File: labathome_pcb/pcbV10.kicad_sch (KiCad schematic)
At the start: 118 parts, among them J1 PROG, J10 Fan1, J11 Fan2, J12 VPS, J15 1B 2A, J18 Power, J2 Srvo, J20 FAN5V, J3 I2C, J4 1wire, J5 EXT, J6 5V 3V GN 24, J7 485, J9 GN 5V RGB GN, K1 G6K-2, K2 G6K-2, K3 G6K-2, Q1 BC817, Q2 BC817, Q4 BC817, Q5 IRLML6344, Q6 BC817, Q7 TIP41, Q9 IRLML6344, SW1 BTN BLUE, SW10 5V FAN 24V, SW12 RESET, SW2 YELLOW, SW3 GREEN, SW4 RED, SW5 BTN WHITE, SW6 OFF TERM ON, SW7 LED HTR, SW8 REL ROT, SW9 SNS MOV, U1 AMS1117, U14 IPS_240_240, U2 ESP32-WROOM-32, U21 BTS462T, U4 CH340C, U6 MAX3485, X1 FAN_6024

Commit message: PCB as ordered at JLCPCB
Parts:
- removed U21: BTS462T, Package_TO_SOT_SMD:TO-252-5_TabPin3, symbol liebler_SEMICONDUCTORS:BTS462T
- added C27: 10u, Capacitor_SMD:C_1206_3216Metric, symbol Device:C
- added C40: u1, Capacitor_SMD:C_0603_1608Metric, symbol Device:C
- added JP8: Fan2toFan1, Jumper:SolderJumper-2_P1.3mm_Open_RoundedPad1.0x1.5mm, symbol Jumper:Jumper_2_Open
- added U16: AS4950, Package_SO:SOIC-8-1EP_3.9x4.9mm_P1.27mm_EP2.29x3mm_ThermalVias, symbol liebler_SEMICONDUCTORS:AS4950
- IMG4: value WHS -> FHOS; footprint liebler_DRAWINGS:LOGO_WHS -> liebler_DRAWINGS:LOGO_FHOS_80mm
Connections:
- net +24V: now also C27.2, C40.2, U16.5 (VP)
- net +3V3: now also U16.4 (Vref)
- net FAN1_DRIVE: now also U16.2 (IN2)
- net FAN2_DRIVE: now also JP8.1 (A)
- net GND: now also C27.1, C40.1, U16.1 (GND), U16.7 (LSEN), U16.9 (PAD); no longer J10.1 (Pin_1)
- net at J10.2 (Pin_2): now also U16.8 (OUT2)
- net VFAN: now reaches J11.2 (Pin_2), SW10.2 (B)
- new net: J10.1 (Pin_1), U16.6 (OUT1)
- new net: JP8.2 (B), U16.3 (IN1)
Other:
- note added: "FAN"
- note removed: "USB->20V"
- moved on the sheet: J10, J11, J20, R9, SW10

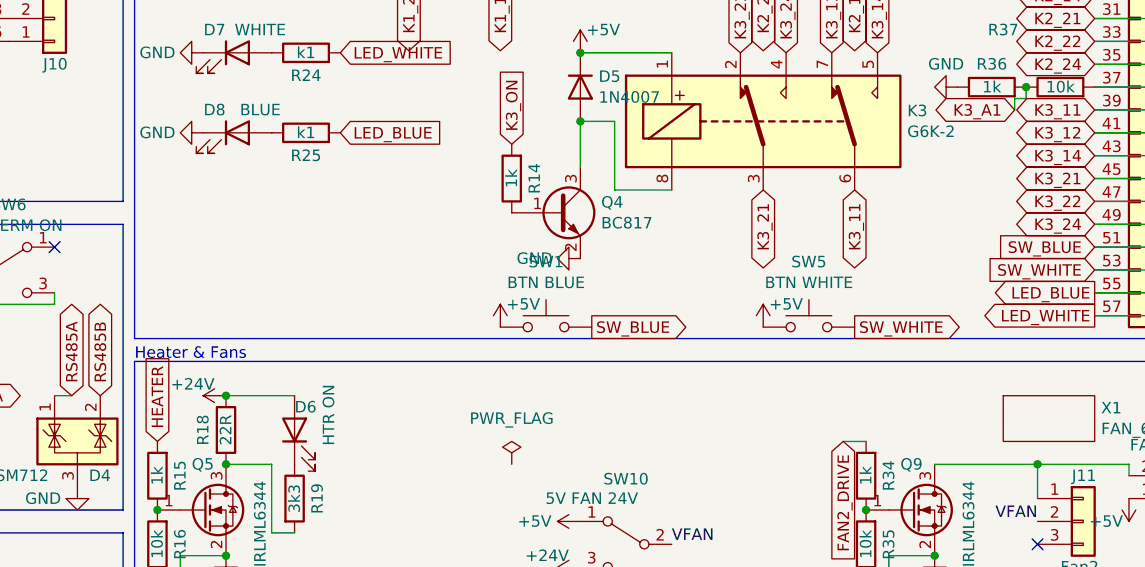
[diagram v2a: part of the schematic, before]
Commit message: LTSpice Simulation & minor optical fixes
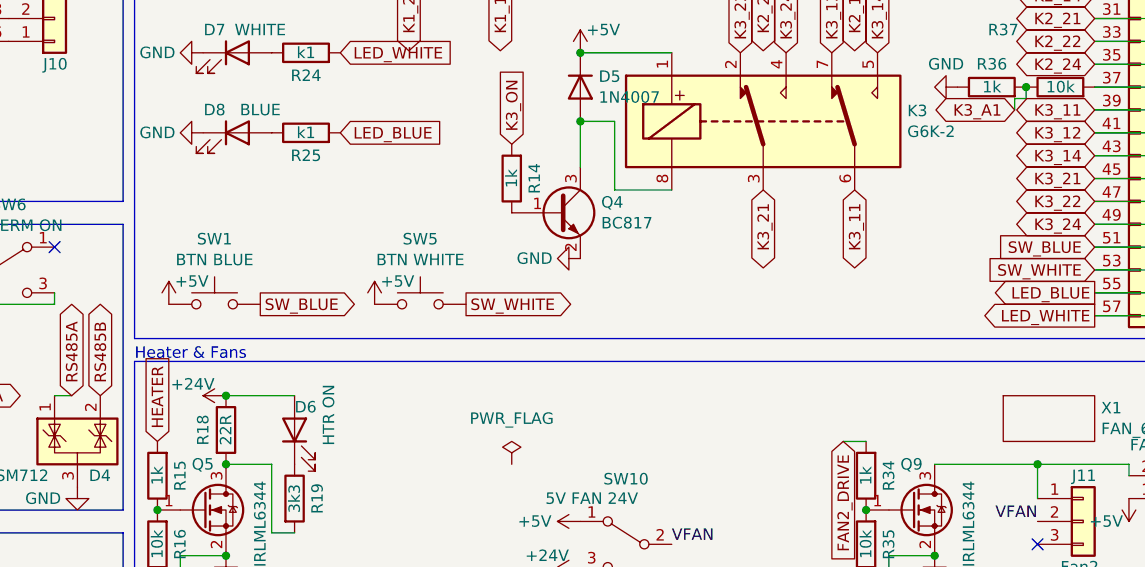
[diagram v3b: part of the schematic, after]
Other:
- moved on the sheet: SW1, SW5
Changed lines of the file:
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@@
     (effects (font (size 1.27 1.27)) (justify right bottom))
   )
-  (global_label "SW_WHITE" (shape output) (at 238.76 80.01 0) (fields_autoplaced)
+  (global_label "SW_WHITE" (shape output) (at 195.58 77.47 0) (fields_autoplaced)
     (effects (font (size 1.27 1.27)) (justify left))
-    (property "Intersheet References" "${INTERSHEET_REFS}" (id 0) (at 0 0 0)
+    (property "Intersheet References" "${INTERSHEET_REFS}" (id 0) (at -43.18 -2.54 0)
       (effects (font (size 1.27 1.27)) hide)
     )
@@
     )
   )
-  (global_label "SW_BLUE" (shape output) (at 209.55 80.01 0) (fields_autoplaced)
+  (global_label "SW_BLUE" (shape output) (at 172.72 77.47 0) (fields_autoplaced)
     (effects (font (size 1.27 1.27)) (justify left))
-    (property "Intersheet References" "${INTERSHEET_REFS}" (id 0) (at 0 0 0)
+    (property "Intersheet References" "${INTERSHEET_REFS}" (id 0) (at -36.83 -2.54 0)
       (effects (font (size 1.27 1.27)) hide)
     )
@@
     (pin "3")
   )
-  (symbol (lib_id "Switch:SW_Push") (at 204.47 80.01 0) (unit 1)
+  (symbol (lib_id "Switch:SW_Push") (at 167.64 77.47 0) (unit 1)
     (in_bom yes) (on_board yes)
-    (property "Reference" "SW1" (id 0) (at 204.47 72.771 0))
-    (property "Value" "BTN BLUE" (id 1) (at 204.47 75.0824 0))
-    (property "Footprint" "liebler_MECH:SW_Push_1P1T_NO_CK_PTS125Sx43PSMTR" (id 2) (at 204.47 74.93 0)
+    (property "Reference" "SW1" (id 0) (at 167.64 70.231 0))
+    (property "Value" "BTN BLUE" (id 1) (at 167.64 72.5424 0))
+    (property "Footprint" "liebler_MECH:SW_Push_1P1T_NO_CK_PTS125Sx43PSMTR" (id 2) (at 167.64 72.39 0)
       (effects (font (size 1.27 1.27)) hide)
     )
-    (property "Datasheet" "~" (id 3) (at 204.47 74.93 0)
+    (property "Datasheet" "~" (id 3) (at 167.64 72.39 0)
       (effects (font (size 1.27 1.27)) hide)
     )
@@
     (pin "1")
   )
-  (symbol (lib_id "power:+5V") (at 199.39 80.01 0) (unit 1)
+  (symbol (lib_id "power:+5V") (at 162.56 77.47 0) (unit 1)
     (in_bom yes) (on_board yes)
-    (property "Reference" "#PWR0168" (id 0) (at 199.39 83.82 0)
+    (property "Reference" "#PWR0168" (id 0) (at 162.56 81.28 0)
       (effects (font (size 1.27 1.27)) hide)
     )
-    (property "Value" "+5V" (id 1) (at 201.93 77.47 0))
-    (property "Footprint" "" (id 2) (at 199.39 80.01 0)
+    (property "Value" "+5V" (id 1) (at 165.1 74.93 0))
+    (property "Footprint" "" (id 2) (at 162.56 77.47 0)
       (effects (font (size 1.27 1.27)) hide)
     )
-    (property "Datasheet" "" (id 3) (at 199.39 80.01 0)
+    (property "Datasheet" "" (id 3) (at 162.56 77.47 0)
       (effects (font (size 1.27 1.27)) hide)
     )
     (pin "1")
   )
-  (symbol (lib_id "Switch:SW_Push") (at 233.68 80.01 0) (unit 1)
+  (symbol (lib_id "Switch:SW_Push") (at 190.5 77.47 0) (unit 1)
     (in_bom yes) (on_board yes)
-    (property "Reference" "SW5" (id 0) (at 233.68 72.771 0))
-    (property "Value" "BTN WHITE" (id 1) (at 233.68 75.0824 0))
-    (property "Footprint" "liebler_MECH:SW_Push_1P1T_NO_CK_PTS125Sx43PSMTR" (id 2) (at 233.68 74.93 0)
+    (property "Reference" "SW5" (id 0) (at 190.5 70.231 0))
+    (property "Value" "BTN WHITE" (id 1) (at 190.5 72.5424 0))
+    (property "Footprint" "liebler_MECH:SW_Push_1P1T_NO_CK_PTS125Sx43PSMTR" (id 2) (at 190.5 72.39 0)
       (effects (font (size 1.27 1.27)) hide)
     )
-    (property "Datasheet" "~" (id 3) (at 233.68 74.93 0)
+    (property "Datasheet" "~" (id 3) (at 190.5 72.39 0)
       (effects (font (size 1.27 1.27)) hide)
     )
@@
     (pin "2")
   )
-  (symbol (lib_id "power:+5V") (at 228.6 80.01 0) (unit 1)
+  (symbol (lib_id "power:+5V") (at 185.42 77.47 0) (unit 1)
     (in_bom yes) (on_board yes)
-    (property "Reference" "#PWR0169" (id 0) (at 228.6 83.82 0)
+    (property "Reference" "#PWR0169" (id 0) (at 185.42 81.28 0)
       (effects (font (size 1.27 1.27)) hide)
     )
-    (property "Value" "+5V" (id 1) (at 231.14 77.47 0))
-    (property "Footprint" "" (id 2) (at 228.6 80.01 0)
+    (property "Value" "+5V" (id 1) (at 187.96 74.93 0))
+    (property "Footprint" "" (id 2) (at 185.42 77.47 0)
       (effects (font (size 1.27 1.27)) hide)
     )
-    (property "Datasheet" "" (id 3) (at 228.6 80.01 0)
+    (property "Datasheet" "" (id 3) (at 185.42 77.47 0)
       (effects (font (size 1.27 1.27)) hide)
     )
@@
     )
     (path "/00000000-0000-0000-0000-000061349a3c/b0f885e6-bad8-4725-9d62-48d952608fb4"
-      (reference "J24") (unit 1) (value "AOUT") (footprint "Connector_JST:JST_XH_S4B-XH-A_1x04_P2.50mm_Horizontal")
+      (reference "J24") (unit 1) (value "24 GN GN OUT") (footprint "Connector_JST:JST_XH_S4B-XH-A_1x04_P2.50mm_Horizontal")
     )
     (path "/00000000-0000-0000-0000-000061349a3c/d729a5b2-efbc-4e67-a1f6-ed7937333728"
